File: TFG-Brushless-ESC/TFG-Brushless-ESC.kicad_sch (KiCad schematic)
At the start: 75 parts, among them J2 USB C Receptacle, J3 HALL SENSORS, J4 SWD-I2C, J5 24V IN, Q7 DMG3402L, SW1 BOOT0, SW2 NRST, U1 LM317L_SOT-89, U11 ADC081C021, U2 LM317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

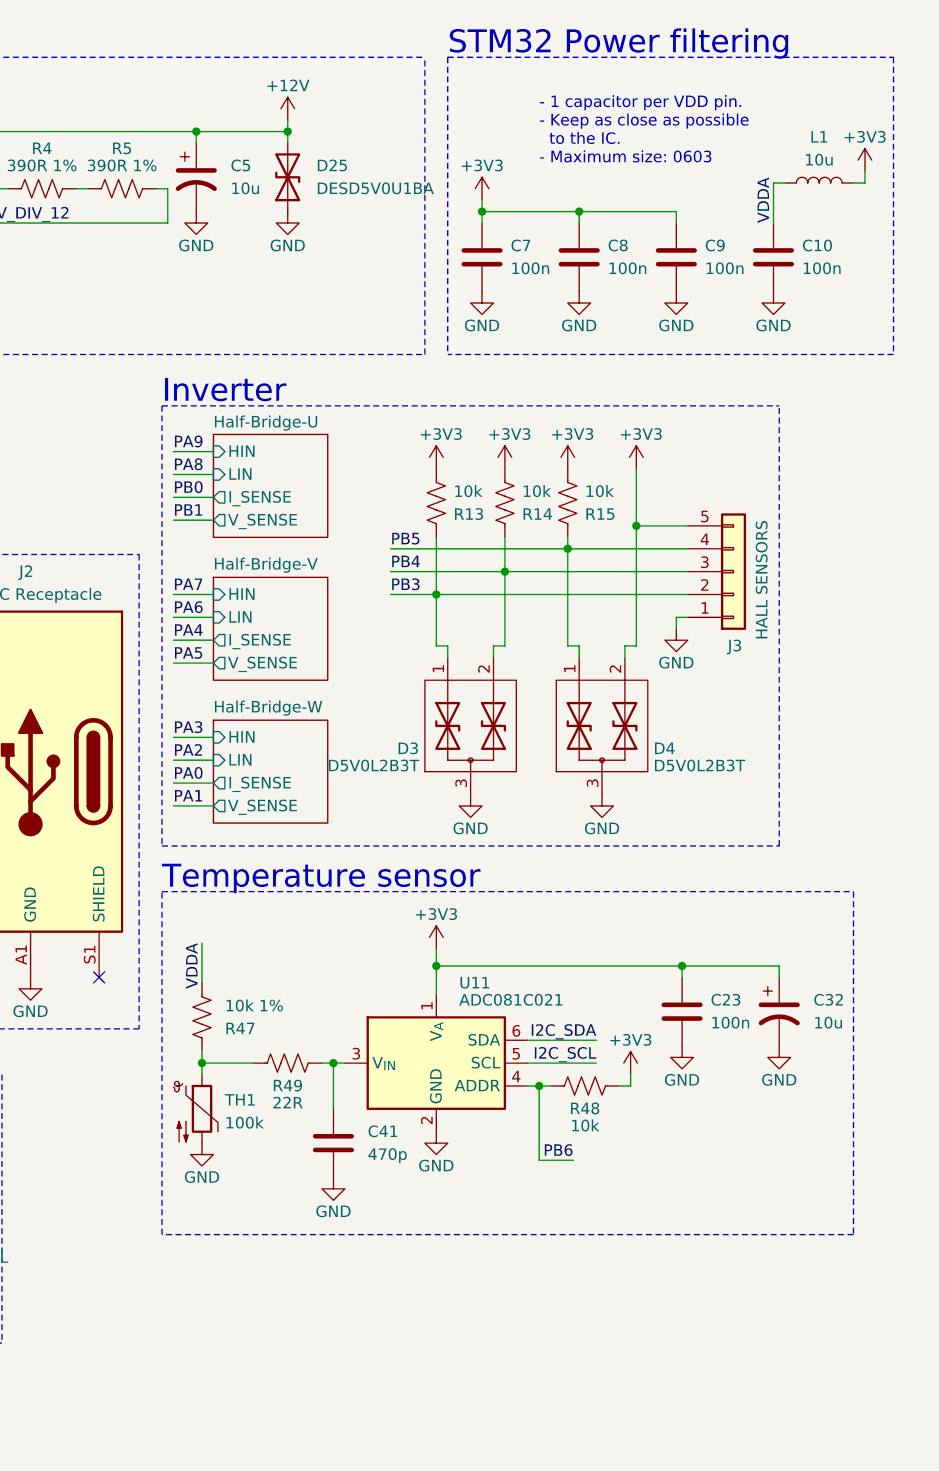
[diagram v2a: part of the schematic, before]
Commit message: Added temperature sensors per phase and adc
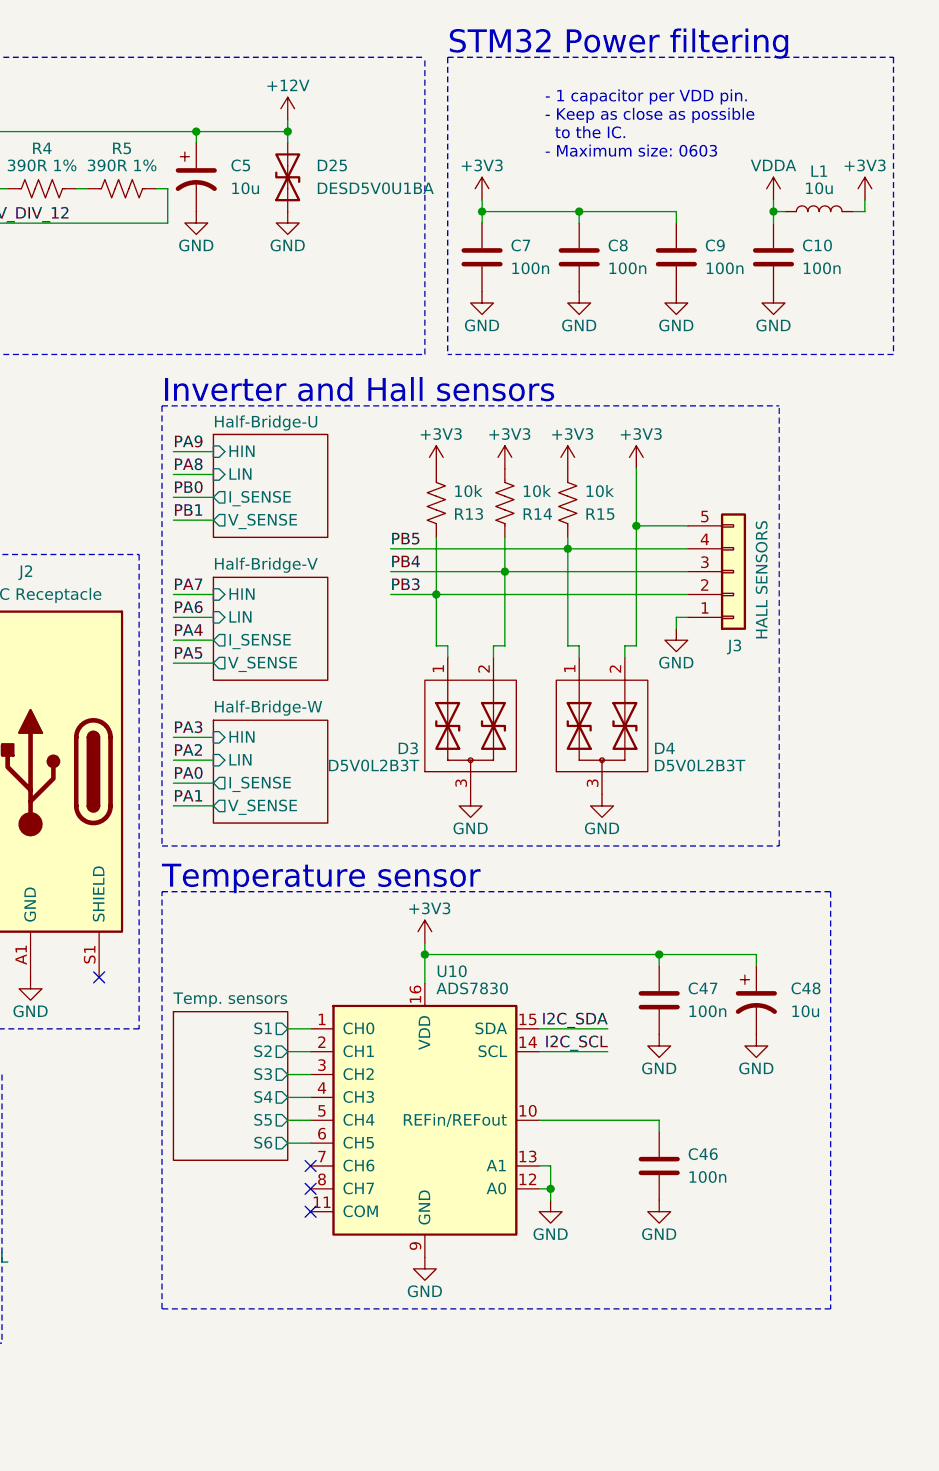
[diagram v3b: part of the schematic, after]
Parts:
- removed C23: 100n, Capacitor_SMD:C_0603_1608Metric, symbol Device:C
- removed C32: 10u, Capacitor_SMD:CP_Elec_4x5.4, symbol Device:C_Polarized_US
- removed C41: 470p, symbol Device:C
- removed R47: 10k 1%, Resistor_SMD:R_0603_1608Metric, symbol Device:R_US
- removed R48: 10k, Resistor_SMD:R_0603_1608Metric, symbol Device:R_US
- removed R49: 22R, Resistor_SMD:R_0603_1608Metric, symbol Device:R_US
- removed TH1: 100k, Connector_PinHeader_1.00mm:PinHeader_1x02_P1.00mm_Vertical, symbol Device:Thermistor_NTC
- removed U11: ADC081C021, Package_TO_SOT_SMD:SOT-23-6, symbol Analog_ADC:ADC101C021CIMK
- added C46, C47: 100n, Capacitor_SMD:C_0603_1608Metric, symbol Device:C
- added C48: 10u, Capacitor_SMD:CP_Elec_4x5.4, symbol Device:C_Polarized_US
- added U10: ADS7830, Package_SO:TSSOP-16_4.4x5mm_P0.65mm, symbol Analog_DAC:ADS7830
- L2: footprint Connector_PinHeader_1.00mm:PinHeader_1x02_P1.00mm_Vertical -> Connector_PinHeader_2.54mm:PinHeader_1x02_P2.54mm_Vertical
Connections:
- net +3V3: now also C47.1, C48.1, U10.16 (VDD)
- net GND: now also C46.2, C47.2, C48.2, U10.12 (A0), U10.13 (A1), U10.9 (GND)
- net I2C_SCL: now also U10.14 (SCL)
- net I2C_SDA: now also U10.15 (SDA)
- new net: C46.1, U10.10 (REFin/REFout)
- new net Temp. sensors/S1: U10.1 (CH0)
- new net Temp. sensors/S2: U10.2 (CH1)
- new net Temp. sensors/S3: U10.3 (CH2)
- new net Temp. sensors/S4: U10.4 (CH3)
- new net Temp. sensors/S5: U10.5 (CH4)
- new net Temp. sensors/S6: U10.6 (CH5)
- no-connect marks 4 -> 7
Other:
- added sheet Temp. sensors (tempSensors.kicad_sch)
- note added: "Inverter and Hall sensors"
- note removed: "Inverter"
- moved on the sheet: L1

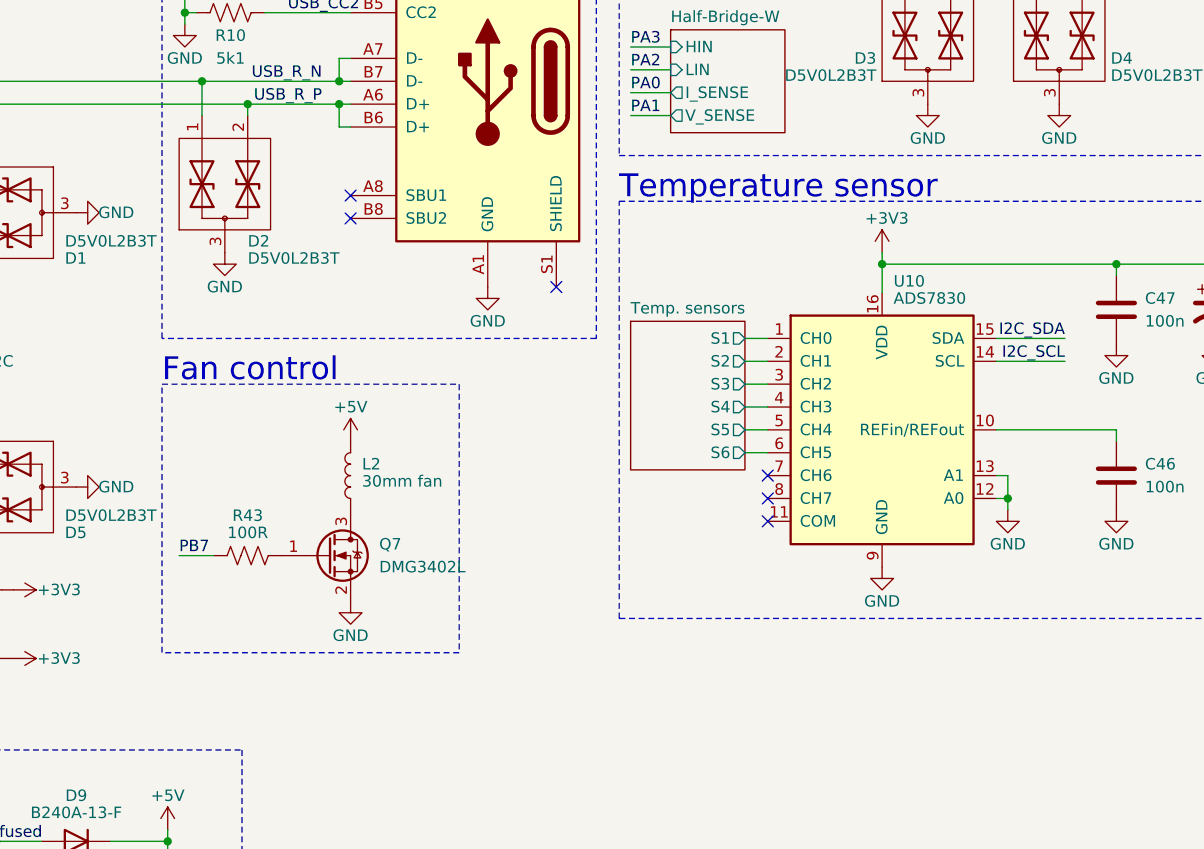
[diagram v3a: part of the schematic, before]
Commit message: Added pulldown resistors for the half bridge mosfets, fan mosfet and fixed code pinout
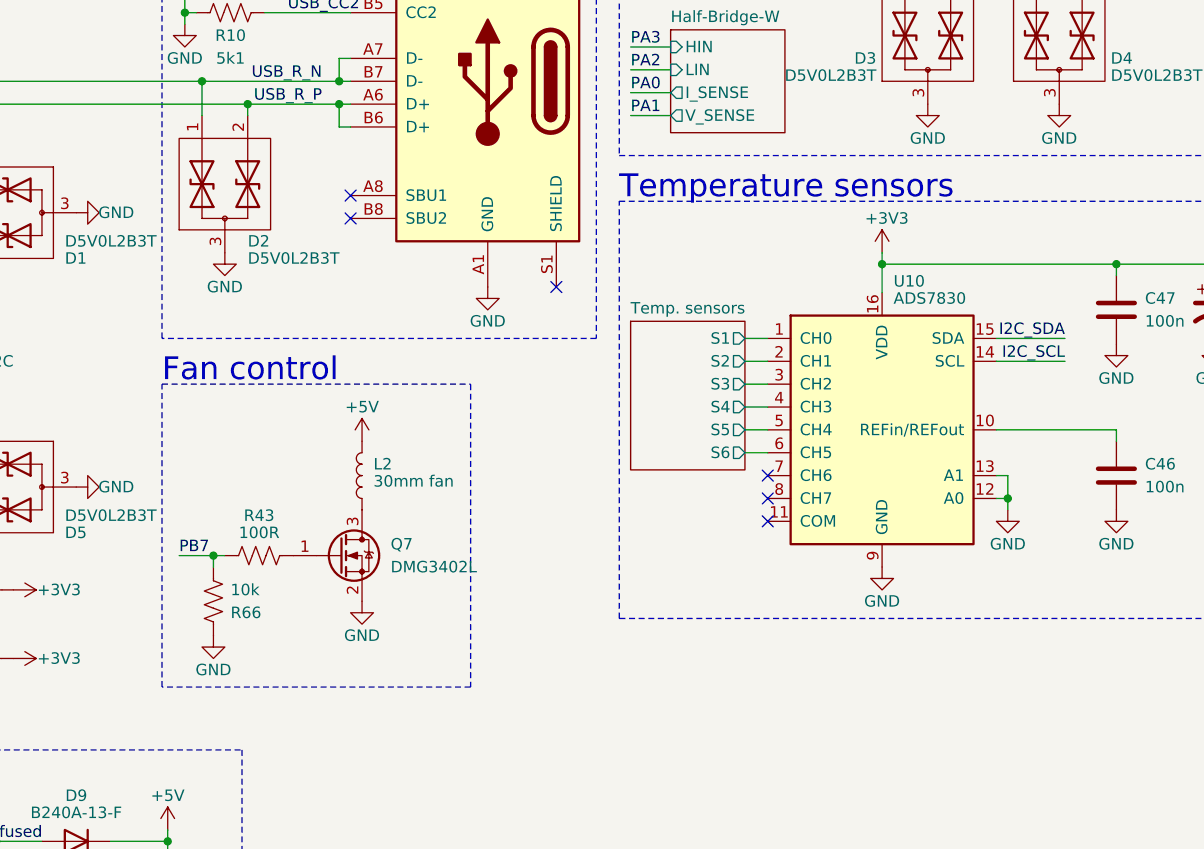
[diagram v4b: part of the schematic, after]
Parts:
- added R66: 10k, Resistor_SMD:R_0603_1608Metric, symbol Device:R_US
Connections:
- net GND: now also R66.1
- net PB7: now also R66.2
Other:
- note added: "Temperature sensors"
- note removed: "Temperature sensor"
- moved on the sheet: L2, Q7, R43
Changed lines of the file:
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@@
 	)
 	(junction
+		(at 155.575 149.86)
+		(diameter 0)
+		(color 0 0 0 0)
+	)
+	(junction
 		(at 88.265 181.61)
 		(diameter 0)
@@
 	(wire
 		(pts
+			(xy 155.575 149.86) (xy 155.575 151.13)
+		)
+		(stroke
+			(width 0)
+			(type default)
+		)
+	)
+	(wire
+		(pts
 			(xy 245.745 71.12) (xy 245.745 72.39)
 		)
@@
 	(wire
 		(pts
+			(xy 155.575 149.86) (xy 156.845 149.86)
+		)
+		(stroke
+			(width 0)
+			(type default)
+		)
+	)
+	(wire
+		(pts
 			(xy 95.25 146.685) (xy 93.98 146.685)
 		)
@@
 	(rectangle
 		(start 149.86 130.81)
-		(end 182.88 160.655)
+		(end 184.15 164.465)
 		(stroke
 			(width 0)
@@
 		)
 	)
-	(text "Temperature sensor"
+	(text "Temperature sensors"
 		(exclude_from_sim no)
 		(at 200.66 110.49 0)
@@
 		(lib_name "+5V_1")
 		(lib_id "power:+5V")
-		(at 170.815 137.16 0)
+		(at 172.085 137.16 0)
 		(unit 1)
 		(exclude_from_sim no)
@@
 		(dnp no)
 		(property "Reference" "#PWR0107"
-			(at 170.815 140.97 0)
+			(at 172.085 140.97 0)
 			(effects
 				(font
@@
 		)
 		(property "Value" "+5V"
-			(at 170.815 133.35 0)
+			(at 172.085 133.35 0)
 			(effects
 				(font
@@
 		)
 		(property "Footprint" ""
-			(at 170.815 137.16 0)
+			(at 172.085 137.16 0)
 			(effects
 				(font
@@
 		)
 		(property "Datasheet" ""
-			(at 170.815 137.16 0)
+			(at 172.085 137.16 0)
 			(effects
 				(font
@@
 		)
 		(property "Description" "Power symbol creates a global label with name \"+5V\""
-			(at 170.815 137.16 0)
+			(at 172.085 137.16 0)
 			(effects
 				(font
@@
 	)
 	(symbol
+		(lib_id "power:GND")
+		(at 155.575 158.75 0)
+		(unit 1)
+		(exclude_from_sim no)
+		(in_bom yes)
+		(on_board yes)
+		(dnp no)
+		(property "Reference" "#PWR0131"
+			(at 155.575 165.1 0)
+			(effects
+				(font
+					(size 1.27 1.27)
+				)
+				(hide yes)
+			)
+		)
+		(property "Value" "GND"
+			(at 155.575 162.56 0)
+			(effects
+				(font
+					(size 1.27 1.27)
+				)
+			)
+		)
+		(property "Footprint" ""
+			(at 155.575 158.75 0)
+			(effects
+				(font
+					(size 1.27 1.27)
+				)
+				(hide yes)
+			)
+		)
+		(property "Datasheet" ""
+			(at 155.575 158.75 0)
+			(effects
+				(font
+					(size 1.27 1.27)
+				)
+				(hide yes)
+			)
+		)
+		(property "Description" ""
+			(at 155.575 158.75 0)
+			(effects
+				(font
+					(size 1.27 1.27)
+				)
+				(hide yes)
+			)
+		)
+		(pin "1"
+		)
+		(instances
+			(project "TFG-Brushless-ESC"
+				(path "/fc8dd9a9-f99a-4338-8182-2c8b4b8ed6dd"
+					(reference "#PWR0131")
+					(unit 1)
+				)
+			)
+		)
+	)
+	(symbol
 		(lib_id "power:+3V3")
 		(at 30.48 150.495 0)
@@
 	(symbol
 		(lib_id "Device:R_US")
+		(at 155.575 154.94 180)
+		(unit 1)
+		(exclude_from_sim no)
+		(in_bom yes)
+		(on_board yes)
+		(dnp no)
+		(property "Reference" "R66"
+			(at 157.48 156.21 0)
+			(effects
+				(font
+					(size 1.27 1.27)
+				)
+				(justify right)
+			)
+		)
+		(property "Value" "10k"
+			(at 157.48 153.67 0)
+			(effects
+				(font
+					(size 1.27 1.27)
+				)
+				(justify right)
+			)
+		)
+		(property "Footprint" "Resistor_SMD:R_0603_1608Metric"
+			(at 154.559 154.686 90)
+			(effects
+				(font
+					(size 1.27 1.27)
+				)
+				(hide yes)
+			)
+		)
+		(property "Datasheet" "~"
+			(at 155.575 154.94 0)
+			(effects
+				(font
+					(size 1.27 1.27)
+				)
+				(hide yes)
+			)
+		)
+		(property "Description" ""
+			(at 155.575 154.94 0)
+			(effects
+				(font
+					(size 1.27 1.27)
+				)
+				(hide yes)
+			)
+		)
+		(pin "1"
+		)
+		(pin "2"
+		)
+		(instances
+			(project "TFG-Brushless-ESC"
+				(path "/fc8dd9a9-f99a-4338-8182-2c8b4b8ed6dd"
+					(reference "R66")
+					(unit 1)
+				)
+			)
+		)
+	)
+	(symbol
+		(lib_id "Device:R_US")
 		(at 178.435 32.385 90)
 		(unit 1)
@@
 	(symbol
 		(lib_id "Device:R_US")
-		(at 159.385 149.86 90)
+		(at 160.655 149.86 90)
 		(unit 1)
 		(exclude_from_sim no)
@@
 		(dnp no)
 		(property "Reference" "R43"
-			(at 159.385 145.415 90)
+			(at 160.655 145.415 90)
 			(effects
 				(font
@@
 		)
 		(property "Value" "100R"
-			(at 159.385 147.32 90)
+			(at 160.655 147.32 90)
 			(effects
 				(font
@@
 		)
 		(property "Footprint" "Resistor_SMD:R_0805_2012Metric"
-			(at 159.639 148.844 90)
+			(at 160.909 148.844 90)
 			(effects
 				(font
@@
 		)
 		(property "Datasheet" "~"
-			(at 159.385 149.86 0)
+			(at 160.655 149.86 0)
 			(effects
 				(font
@@
 		)
 		(property "Description" ""
-			(at 159.385 149.86 0)
+			(at 160.655 149.86 0)
 			(effects
 				(font
@@
 		)
 		(property "Sim.Device" "R"
-			(at 159.385 149.86 0)
+			(at 160.655 149.86 0)
 			(effects
 				(font
@@
 		)
 		(property "Sim.Pins" "1=+ 2=-"
-			(at 159.385 149.86 0)
+			(at 160.655 149.86 0)
 			(effects
 				(font
@@
 	(symbol
 		(lib_id "power:GND")
-		(at 170.815 154.94 0)
+		(at 172.085 154.94 0)
 		(unit 1)
 		(exclude_from_sim no)
@@
 		(dnp no)
 		(property "Reference" "#PWR0108"
-			(at 170.815 161.29 0)
+			(at 172.085 161.29 0)
 			(effects
 				(font
@@
 		)
 		(property "Value" "GND"
-			(at 170.815 158.75 0)
+			(at 172.085 158.75 0)
 			(effects
 				(font
@@
 		)
 		(property "Footprint" ""
-			(at 170.815 154.94 0)
+			(at 172.085 154.94 0)
 			(effects
 				(font
@@
 		)
 		(property "Datasheet" ""
-			(at 170.815 154.94 0)
+			(at 172.085 154.94 0)
 			(effects
 				(font
@@
 		)
 		(property "Description" ""
-			(at 170.815 154.94 0)
+			(at 172.085 154.94 0)
 			(effects
 				(font
@@
 	(symbol
 		(lib_id "Transistor_FET:DMG3402L")
-		(at 168.275 149.86 0)
+		(at 169.545 149.86 0)
 		(unit 1)
 		(exclude_from_sim no)
@@
 		(fields_autoplaced yes)
 		(property "Reference" "Q7"
-			(at 173.99 148.5899 0)
+			(at 175.26 148.5899 0)
 			(effects
 				(font
@@
 		)
 		(property "Value" "DMG3402L"
-			(at 173.99 151.1299 0)
+			(at 175.26 151.1299 0)
 			(effects
 				(font
@@
 		)
 		(property "Footprint" "Package_TO_SOT_SMD:SOT-23"
-			(at 173.355 151.765 0)
+			(at 174.625 151.765 0)
 			(effects
 				(font
@@
 		)
 		(property "Datasheet" "http://www.diodes.com/assets/Datasheets/DMG3402L.pdf"
-			(at 173.355 153.67 0)
+			(at 174.625 153.67 0)
 			(effects
 				(font
@@
 		)
 		(property "Description" "4A Id, 30V Vds, N-Channel MOSFET, SOT-23"
-			(at 168.275 149.86 0)
+			(at 169.545 149.86 0)
 			(effects
 				(font
@@
 	(symbol
 		(lib_id "Device:L")
-		(at 170.815 140.97 180)
+		(at 172.085 140.97 180)
 		(unit 1)
 		(exclude_from_sim no)
@@
 		(dnp no)
 		(property "Reference" "L2"
-			(at 172.085 139.7 0)
+			(at 173.355 139.7 0)
 			(effects
 				(font
@@
 		)
 		(property "Value" "30mm fan"
-			(at 172.085 141.605 0)
+			(at 173.355 141.605 0)
 			(effects
 				(font
@@
 		)
 		(property "Footprint" "Connector_PinHeader_2.54mm:PinHeader_1x02_P2.54mm_Vertical"
-			(at 170.815 140.97 0)
+			(at 172.085 140.97 0)
 			(effects
 				(font
@@
 		)
 		(property "Datasheet" "~"
-			(at 170.815 140.97 0)
+			(at 172.085 140.97 0)
 			(effects
 				(font
@@
 		)
 		(property "Description" "Inductor"
-			(at 170.815 140.97 0)
+			(at 172.085 140.97 0)
 			(effects
 				(font

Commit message: Traducción nombres
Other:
- note added: "Boot y Reset"
- note added: "Control ventilador"
- note added: "Filtro alimentación STM32"
- note added: "HSE y LSE"
- note added: "Inversor y sensores Hall"
- note added: "Protección de conectores"
- note added: "Puerto USB CDC"
- note added: "Regulador de 12V"
- note added: "Regulador de 3.3V"
- note added: "Sensores de temperatura y ADC"
- note removed: "12V Regulator"
- note removed: "3.3V Regulator"
- note removed: "Boot & Reset"
- note removed: "Connector protections"
- note removed: "Fan control"
- note removed: "HSE & LSE"
- note removed: "Inverter and Hall sensors"
- note removed: "STM32 Power filtering"
- note removed: "Temperature sensors"
- note removed: "USB CDC Port"
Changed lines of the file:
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@@
 		)
 	)
-	(text "Fan control"
+	(text "Control ventilador"
 		(exclude_from_sim no)
 		(at 149.86 130.81 0)
@@
 		)
 	)
-	(text "Boot & Reset\n"
+	(text "Boot y Reset\n"
 		(exclude_from_sim no)
 		(at 15.875 17.78 0)
@@
 		)
 	)
-	(text "3.3V Regulator"
+	(text "Regulador de 3.3V"
 		(exclude_from_sim no)
 		(at 59.055 17.78 0)
@@
 		)
 	)
-	(text "STM32 Power filtering"
+	(text "Filtro alimentación STM32"
 		(exclude_from_sim no)
 		(at 232.41 17.78 0)
@@
 		)
 	)
-	(text "Connector protections"
+	(text "Protección de conectores"
 		(exclude_from_sim no)
 		(at 46.99 171.45 0)
@@
 		)
 	)
-	(text "Inverter and Hall sensors"
+	(text "Inversor y sensores Hall"
 		(exclude_from_sim no)
 		(at 200.66 56.515 0)
@@
 		)
 	)
-	(text "USB CDC Port\n"
+	(text "Puerto USB CDC\n"
 		(exclude_from_sim no)
 		(at 149.86 73.025 0)
@@
 		)
 	)
-	(text "Temperature sensors"
+	(text "Sensores de temperatura y ADC"
 		(exclude_from_sim no)
 		(at 200.66 110.49 0)
@@
 		)
 	)
-	(text "12V Regulator"
+	(text "Regulador de 12V"
 		(exclude_from_sim no)
 		(at 137.16 17.78 0)
@@
 		)
 	)
-	(text "HSE & LSE"
+	(text "HSE y LSE"
 		(exclude_from_sim no)
 		(at 15.24 77.47 0)
